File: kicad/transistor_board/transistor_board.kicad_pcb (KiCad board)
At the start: 2 copper layers, 25.4 x 38.1 mm, 15 parts, among them J1 Conn_01x10, Q1 MMBF170, Q2 MMBF170, Q3 MMBF170, Q4 MMBF170, U2 ESP32-cam, U3 LM7805_TO220

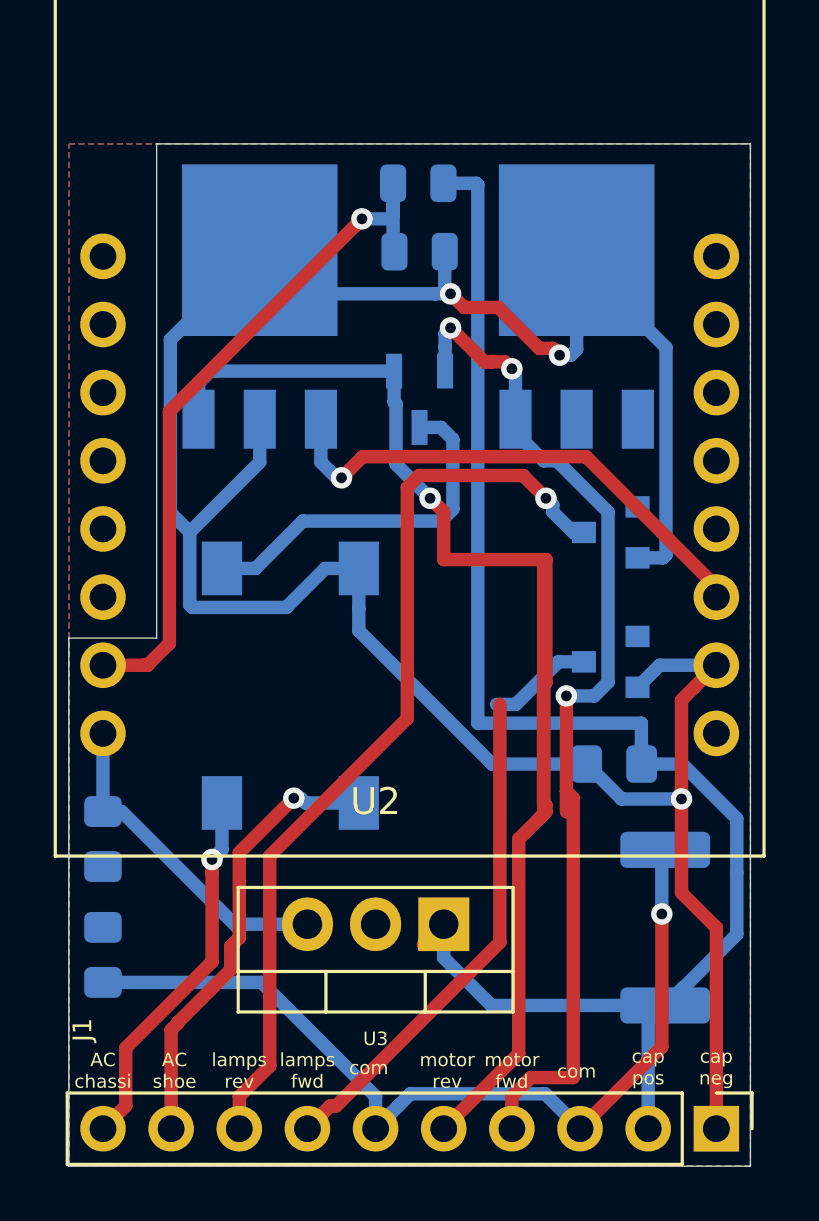
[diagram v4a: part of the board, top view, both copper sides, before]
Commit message: routing on transistor board
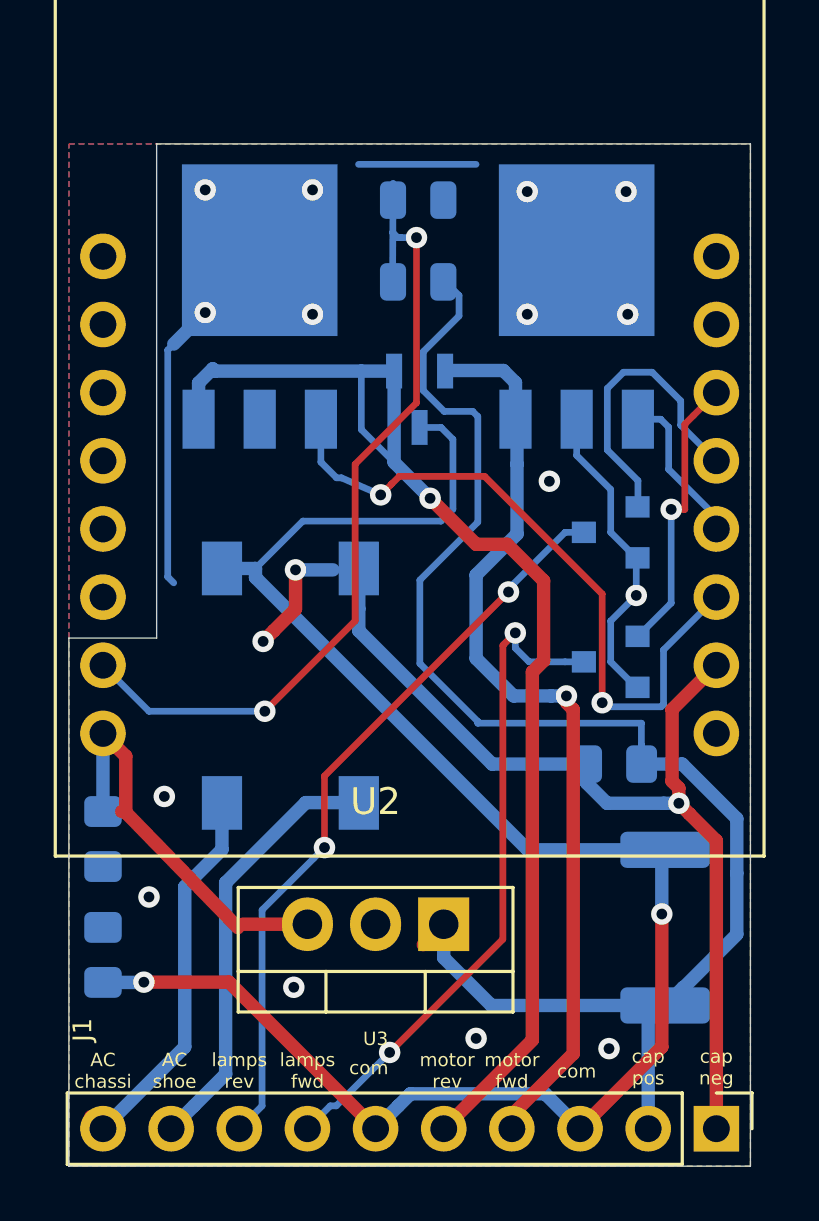
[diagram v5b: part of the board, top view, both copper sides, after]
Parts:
- moved R2 3.68 mm to (126.0, 102.4)
- moved R3 1.92 mm to (126.0, 99.4)
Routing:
- net GND: track 99.0 -> 68.8 mm, vias 3 -> 18
- net Net-(C3-Pad1): track 47.1 -> 66.3 mm, vias 1 -> 2
- net Net-(D3-Pad1): track 62.8 -> 45.7 mm
- net Net-(Q4-Pad1): track 0.00 -> 11.1 mm
- net Net-(Q3-Pad1): track 0.08 -> 10.7 mm, vias 0 -> 1
- net Net-(Q1-Pad1): track 19.3 -> 25.8 mm, vias 1 -> 2
- net Net-(J1-Pad8): track 34.4 -> 28.1 mm, vias 1 -> 2
- net Net-(Q2-Pad1): track 0.00 -> 5.80 mm
- net Net-(D3-Pad2): track 38.7 -> 34.8 mm, vias 3 -> 1
- net Net-(C5-Pad1): track 13.1 -> 15.5 mm
- net Net-(J1-Pad7): track 22.8 -> 25.2 mm, vias 0 -> 2
- net Net-(R2-Pad2): track 29.4 -> 31.1 mm, vias 1 -> 2
- net Net-(C6-Pad2): track 61.9 -> 61.0 mm
- net Net-(D1-Pad3): track 16.8 -> 16.3 mm, vias 1 -> 0
- net Net-(D1-Pad4): vias 1 -> 0
- added copper zone on F.Cu, net GND
- removed copper zone on F.Cu, net Net-(C3-Pad1)
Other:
- board text added: "Henrik & Johan Bjorkman www.drekkar.com 2020-10-01"
- board text removed: "Henrik & Johan Bjorkman www.drekkar.com 2020-09-14"

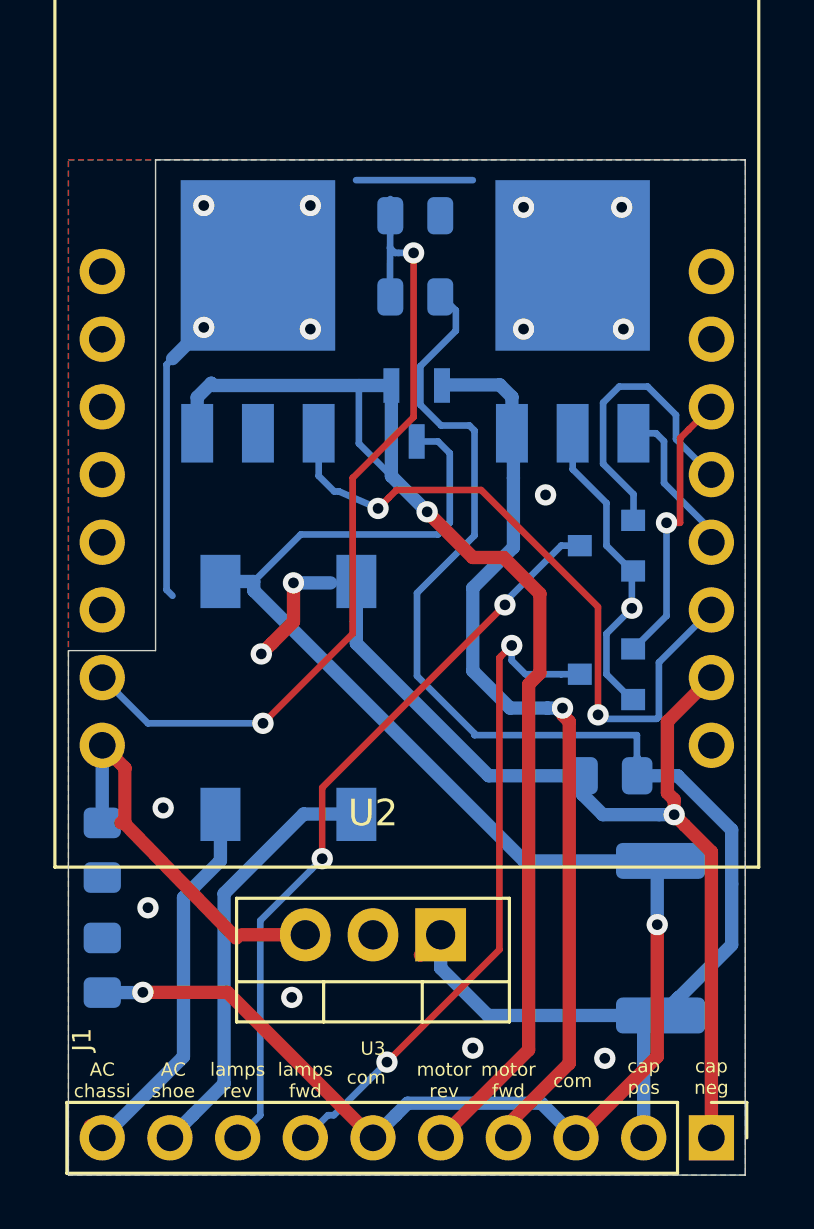
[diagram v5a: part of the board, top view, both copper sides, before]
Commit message: Using ESP32-Cam with 10 pin footprint
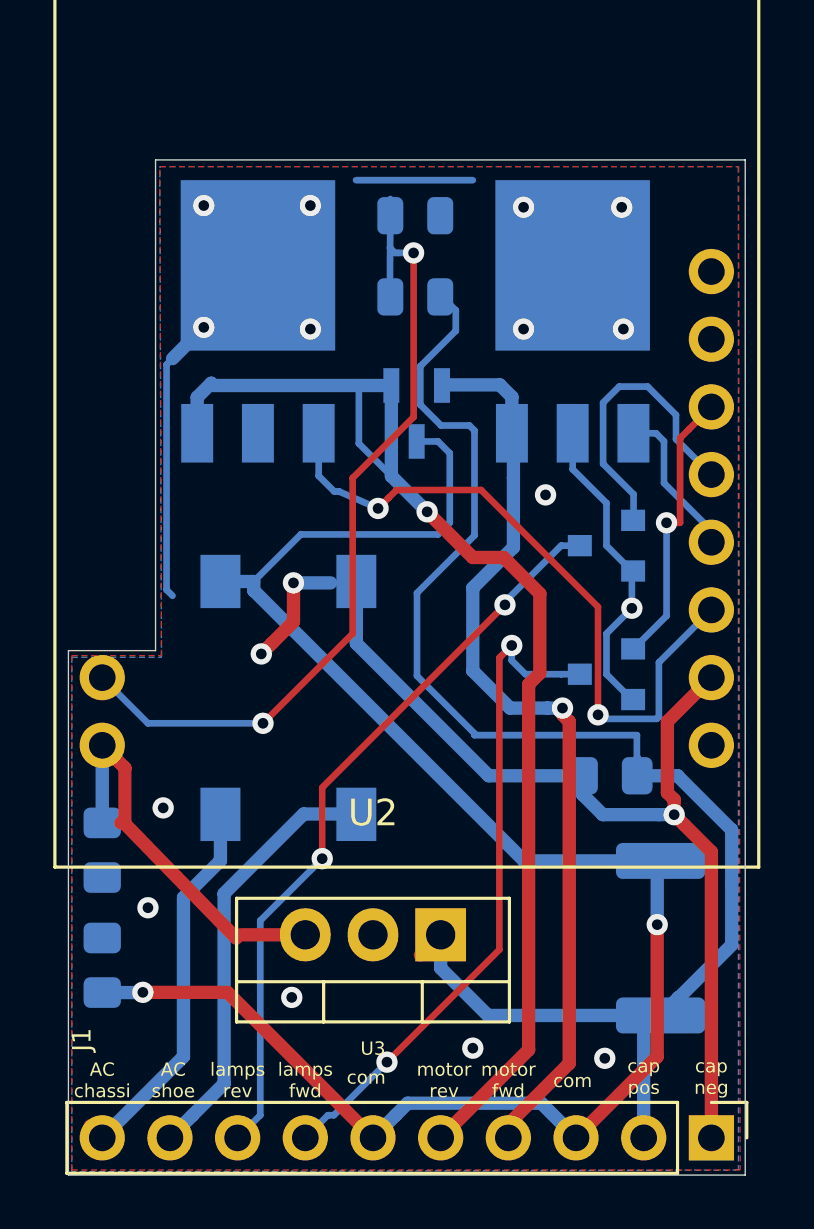
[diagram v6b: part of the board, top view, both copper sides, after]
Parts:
- U2: footprint eit_footprints:ESP32-CAM -> eit_footprints:ESP32-CAM-10pin
